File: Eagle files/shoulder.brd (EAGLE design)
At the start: 28.9 x 24.1 mm, 7 parts

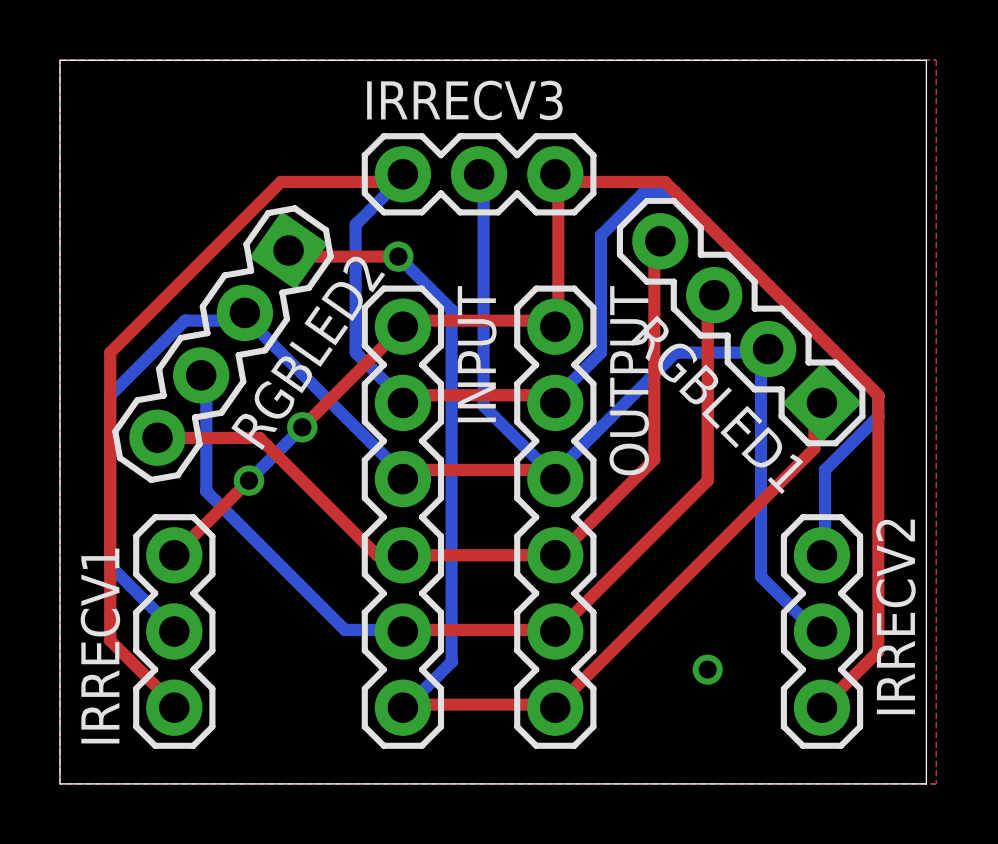
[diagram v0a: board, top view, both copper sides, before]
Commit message: Minor fixes
Added + and - on a few things to help differentiate what is what and
when we need to flip the ribbon cable.
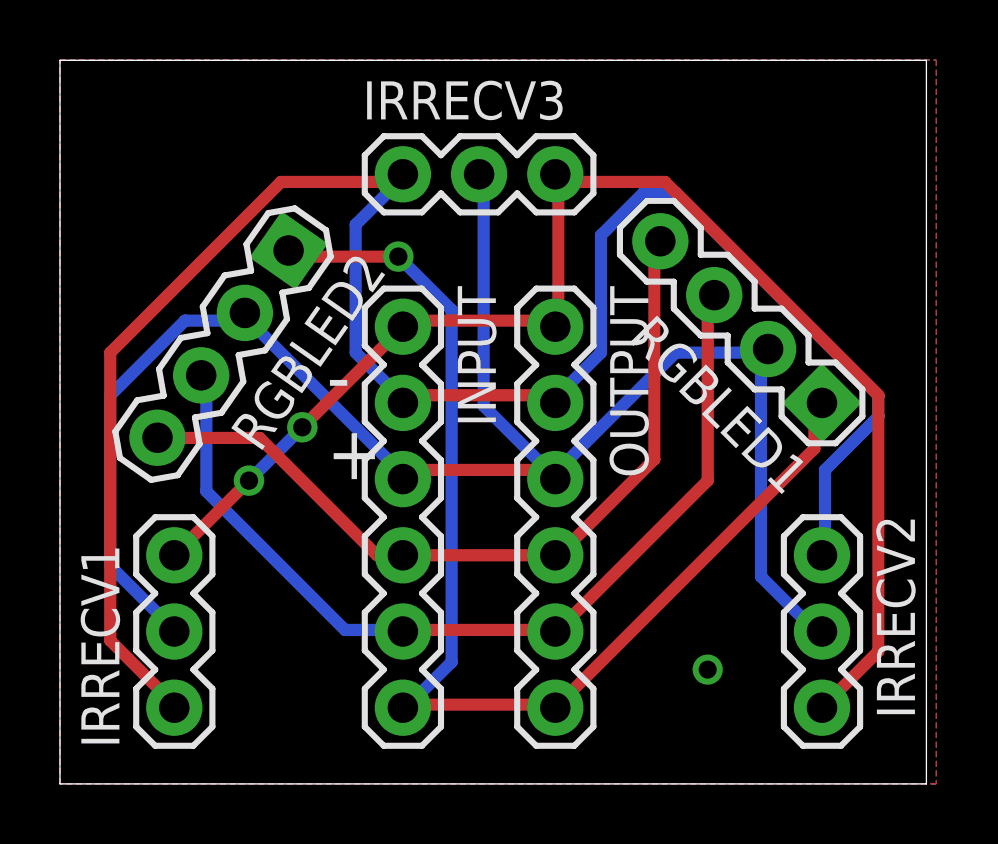
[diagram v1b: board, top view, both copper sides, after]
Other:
- board text added: "+"
- board text added: "-"
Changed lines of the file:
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@@
 V1.0 Greg Tighe
 Lazer Tag</text>
+<text x="13.97" y="13.97" size="1.778" layer="25">-</text>
+<text x="13.97" y="11.43" size="1.778" layer="25">+</text>
 </plain>
 <attributes>

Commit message: aaaaaaaaaaaaaaaaaaaaaaaaaaaaaaaaaaaa
Cleaned up schematics, replaced wire solder points with header pin
mounts for standardization, recreated a broken file and dealt with the
confusion and insanity that followed.
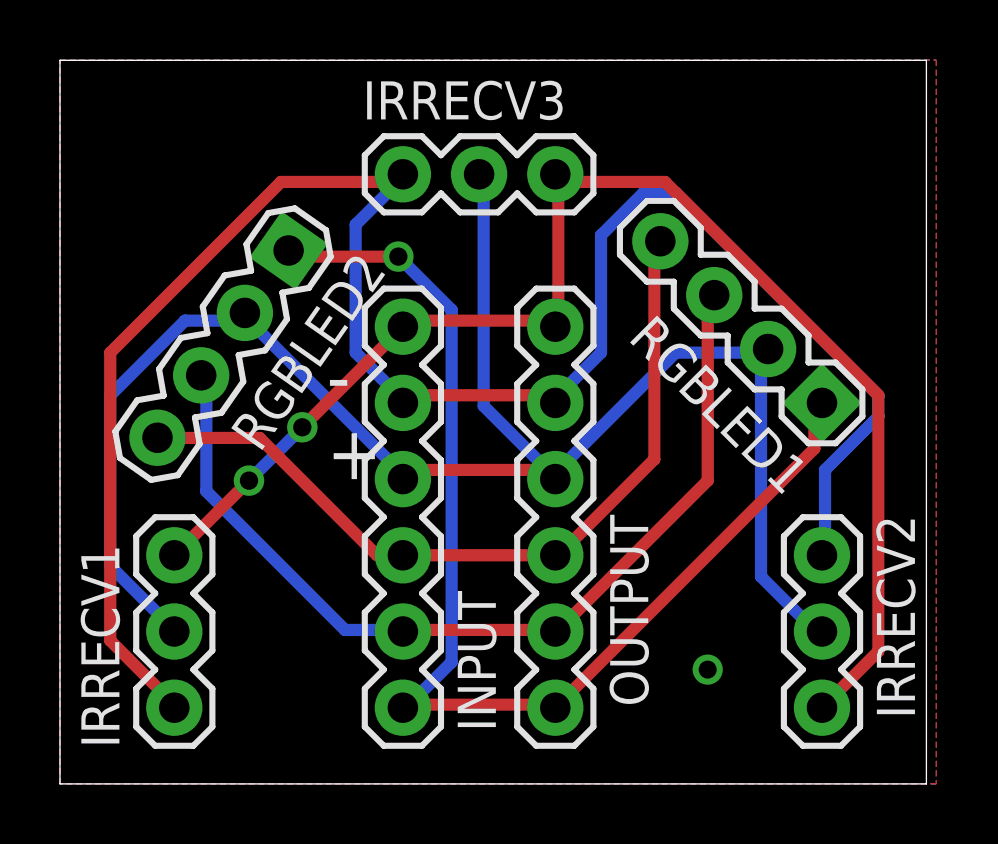
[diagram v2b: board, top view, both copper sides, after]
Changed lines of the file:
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@@
 <layer number="27" name="tValues" color="7" fill="1" visible="yes" active="yes"/>
 <layer number="28" name="bValues" color="7" fill="1" visible="yes" active="yes"/>
-<layer number="29" name="tStop" color="7" fill="3" visible="no" active="yes"/>
-<layer number="30" name="bStop" color="7" fill="6" visible="no" active="yes"/>
-<layer number="31" name="tCream" color="7" fill="4" visible="no" active="yes"/>
-<layer number="32" name="bCream" color="7" fill="5" visible="no" active="yes"/>
-<layer number="33" name="tFinish" color="6" fill="3" visible="no" active="yes"/>
-<layer number="34" name="bFinish" color="6" fill="6" visible="no" active="yes"/>
-<layer number="35" name="tGlue" color="7" fill="4" visible="no" active="yes"/>
-<layer number="36" name="bGlue" color="7" fill="5" visible="no" active="yes"/>
-<layer number="37" name="tTest" color="7" fill="1" visible="no" active="yes"/>
-<layer number="38" name="bTest" color="7" fill="1" visible="no" active="yes"/>
+<layer number="29" name="tStop" color="7" fill="3" visible="yes" active="yes"/>
+<layer number="30" name="bStop" color="7" fill="6" visible="yes" active="yes"/>
+<layer number="31" name="tCream" color="7" fill="4" visible="yes" active="yes"/>
+<layer number="32" name="bCream" color="7" fill="5" visible="yes" active="yes"/>
+<layer number="33" name="tFinish" color="6" fill="3" visible="yes" active="yes"/>
+<layer number="34" name="bFinish" color="6" fill="6" visible="yes" active="yes"/>
+<layer number="35" name="tGlue" color="7" fill="4" visible="yes" active="yes"/>
+<layer number="36" name="bGlue" color="7" fill="5" visible="yes" active="yes"/>
+<layer number="37" name="tTest" color="7" fill="1" visible="yes" active="yes"/>
+<layer number="38" name="bTest" color="7" fill="1" visible="yes" active="yes"/>
 <layer number="39" name="tKeepout" color="4" fill="11" visible="yes" active="yes"/>
 <layer number="40" name="bKeepout" color="1" fill="11" visible="yes" active="yes"/>
@@
 <layer number="42" name="bRestrict" color="1" fill="10" visible="yes" active="yes"/>
 <layer number="43" name="vRestrict" color="2" fill="10" visible="yes" active="yes"/>
-<layer number="44" name="Drills" color="7" fill="1" visible="no" active="yes"/>
-<layer number="45" name="Holes" color="7" fill="1" visible="no" active="yes"/>
-<layer number="46" name="Milling" color="3" fill="1" visible="no" active="yes"/>
-<layer number="47" name="Measures" color="7" fill="1" visible="no" active="yes"/>
+<layer number="44" name="Drills" color="7" fill="1" visible="yes" active="yes"/>
+<layer number="45" name="Holes" color="7" fill="1" visible="yes" active="yes"/>
+<layer number="46" name="Milling" color="3" fill="1" visible="yes" active="yes"/>
+<layer number="47" name="Measures" color="7" fill="1" visible="yes" active="yes"/>
 <layer number="48" name="Document" color="7" fill="1" visible="yes" active="yes"/>
 <layer number="49" name="Reference" color="7" fill="1" visible="yes" active="yes"/>
@@
 </autorouter>
 <elements>
-<element name="INPUT" library="SparkFun-Connectors" package="1X06" value="" x="16.51" y="16.51" rot="R270">
+<element name="INPUT" library="SparkFun-Connectors" package="1X06" value="" x="16.51" y="16.51" smashed="yes" rot="R270">
 <attribute name="PROD_ID" value="CONN-08437" x="16.51" y="16.51" size="1.778" layer="27" rot="R270" display="off"/>
+<attribute name="NAME" x="18.3388" y="7.6962" size="1.27" layer="25" ratio="10" rot="R270"/>
+<attribute name="VALUE" x="13.335" y="17.78" size="1.27" layer="27" rot="R270"/>
 </element>
 <element name="IRRECV1" library="SparkFun-Connectors" package="1X03" value="" x="8.89" y="3.81" rot="R90"/>
 <element name="IRRECV2" library="SparkFun-Connectors" package="1X03" value="" x="30.48" y="8.89" rot="R270"/>
 <element name="IRRECV3" library="SparkFun-Connectors" package="1X03" value="" x="16.51" y="21.59"/>
-<element name="OUTPUT" library="SparkFun-Connectors" package="1X06" value="" x="21.59" y="16.51" rot="R270">
+<element name="OUTPUT" library="SparkFun-Connectors" package="1X06" value="" x="21.59" y="16.51" smashed="yes" rot="R270">
 <attribute name="PROD_ID" value="CONN-08437" x="21.59" y="16.51" size="1.778" layer="27" rot="R270" display="off"/>
+<attribute name="NAME" x="23.4188" y="10.2362" size="1.27" layer="25" ratio="10" rot="R270"/>
+<attribute name="VALUE" x="18.415" y="17.78" size="1.27" layer="27" rot="R270"/>
 </element>
 <element name="RGBLED1" library="SparkFun-Connectors" package="1X04" value="" x="30.48" y="13.97" rot="R135">
